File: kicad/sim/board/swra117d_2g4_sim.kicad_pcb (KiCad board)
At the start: 2 copper layers, 40 x 30 mm, 2 parts, among them P1 50R port

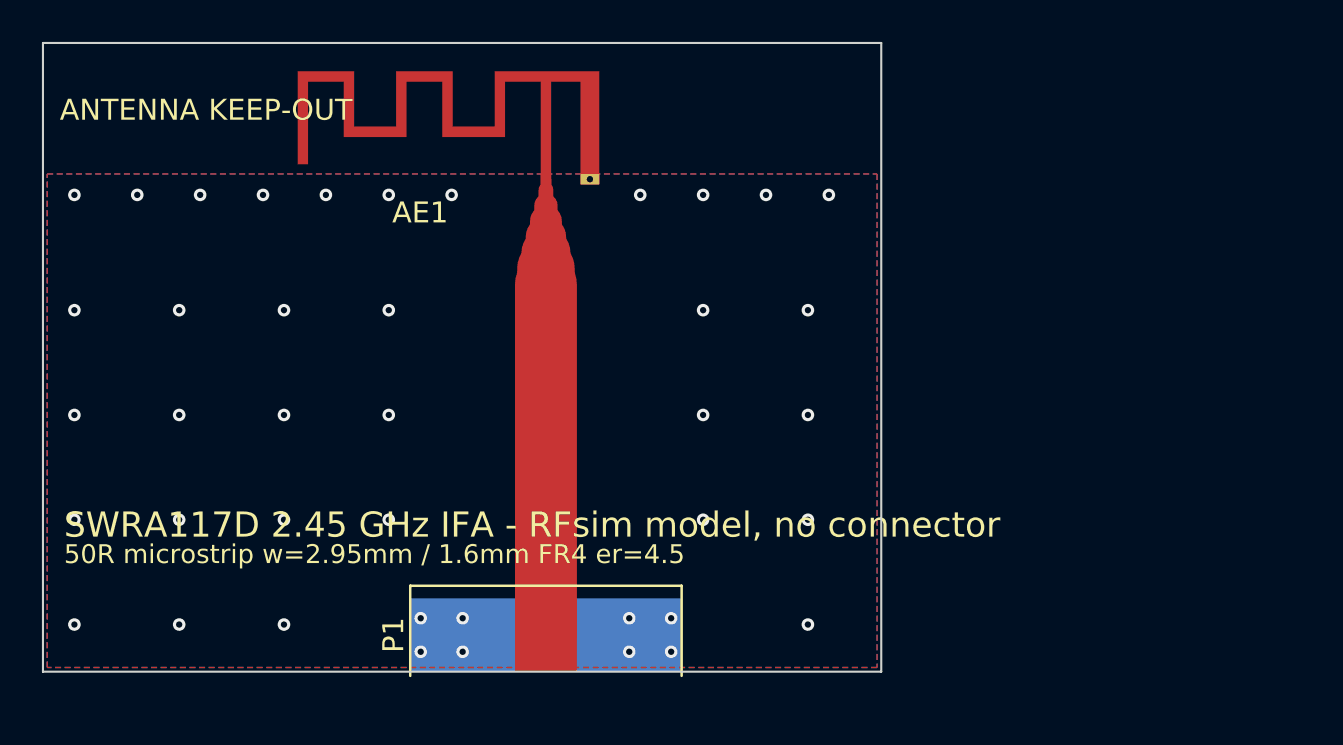
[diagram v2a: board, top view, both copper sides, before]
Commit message: RFsim project: ground on layer 2 only, as SWRA117D Figure 3 draws it
Figure 3 is a two layer board where layer 1 carries the antenna and the feed
and the ground is the grey area captioned "Ground Layer 2" - layer 2 and
nowhere else.  There is no ground copper on the top layer at all, and exactly
one via in the whole drawing: "Via to ground", the W1 = 0.90 mm pad that
shorts the inverted-F.  The simulation project is now that arrangement.  The
fabrication project, with its SMA, is untouched.

One change, three arguments settled:

  * no coplanar copper anywhere near the line, so the feed is unambiguously a
    microstrip over layer 2 and MSL is the port model with nothing left to
    debate;
  * no top pour, so no pour islands to resonate and nothing to stitch - the
    board's only via is the antenna's own, which is what the figure shows;
  * the port's reference is the plane itself, directly under the signal pad,
    rather than a second sheet of copper that has to be tied to it.

The openEMS model reads which layers actually carry ground and builds only
those: it had been adding a top pour unconditionally, which on this board
would have turned the feed into a coplanar line and answered a different
question than the figure asks.

check_sim_board.py now fails on a pour outside B.Cu, on any via at all (the
antenna's ground pad is a pad, not a via), and on that pad ceasing to be a
plated through hole - Figure 3's short.  plane_edge returns None rather than
throwing when a board has no pour, so a deleted plane is reported instead of
crashing the checker; mutate_sim_board.py counts that case as CRASHED, not
caught, which is how it was found.  18 mutations, 18 caught.
stitching_span.py reports "nothing to stitch" for a single-layer ground
instead of aborting.

Co-Authored-By: Claude Opus 5 <noreply@anthropic.com>
Claude-Session: https://claude.ai/code/session_01Prj6bUQ2KQzzxzD4bgtswJ
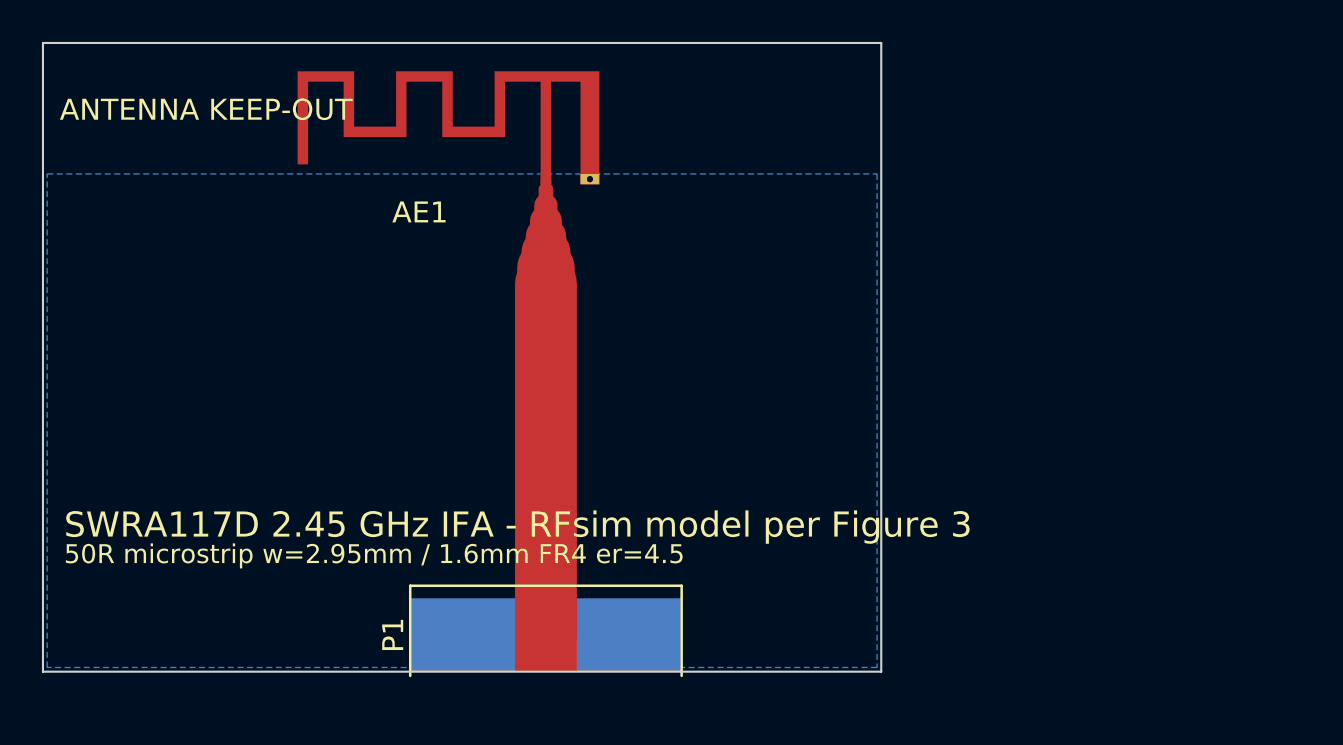
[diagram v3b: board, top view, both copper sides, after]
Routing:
- net GND: vias 41 -> 0
- removed copper zone on F.Cu, net GND
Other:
- board text added: "GROUND IS LAYER 2 (B.Cu) ONLY - no ground copper on F.Cu, and the only via is the antenna's own"
- board text added: "PORT 1: P1 pad 1 over its B.Cu ground pad - microstrip (MSL), not CPW"
- board text added: "SWRA117D 2.45 GHz IFA - RFsim model per Figure 3"
- board text removed: "PORT 1: P1 pad 1, referenced to its B.Cu ground pad - microstrip (MSL), not CPW: no coplanar ground here"
- board text removed: "SWRA117D 2.45 GHz IFA - RFsim model, no connector"
